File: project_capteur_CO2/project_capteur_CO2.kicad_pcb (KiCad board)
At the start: 2 copper layers, 9 parts, among them U1 ESP32_NODEMCU, U2 DHT11

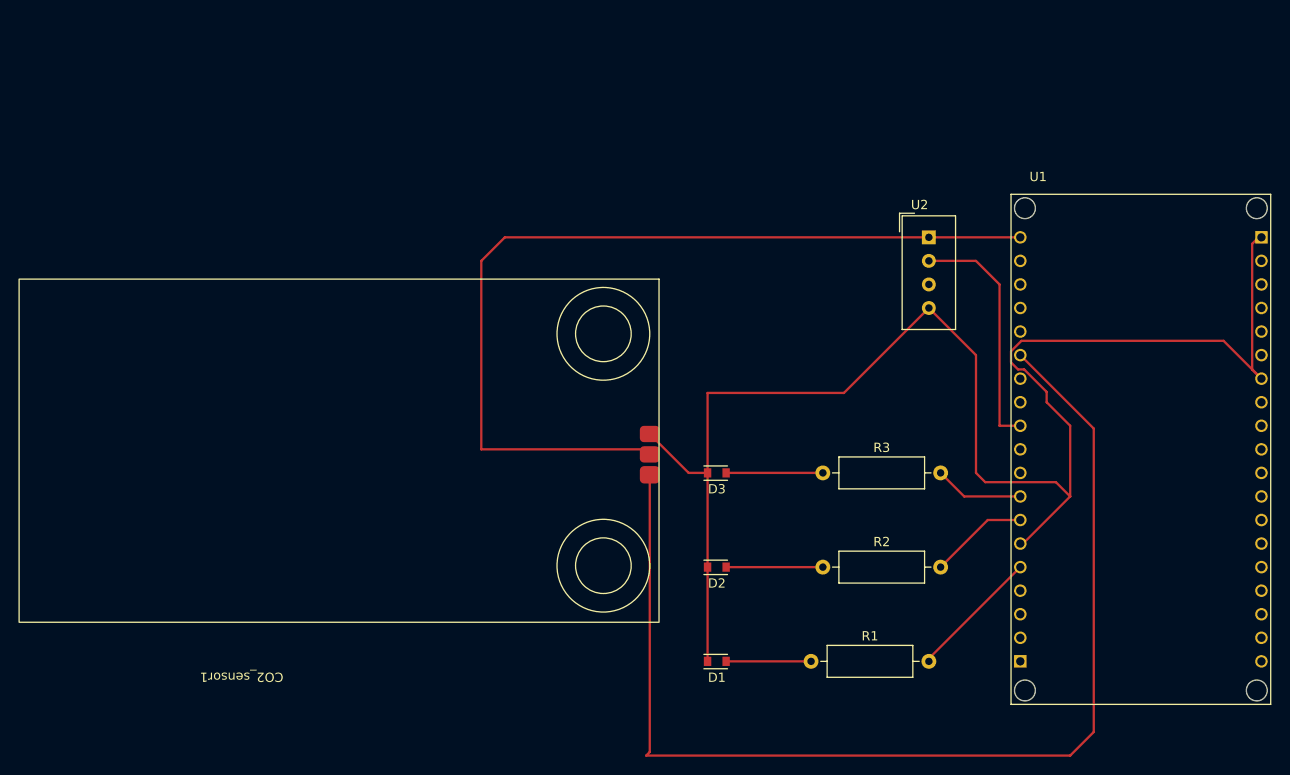
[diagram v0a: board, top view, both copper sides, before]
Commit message: pinheader - coorection led empreinte ajouter
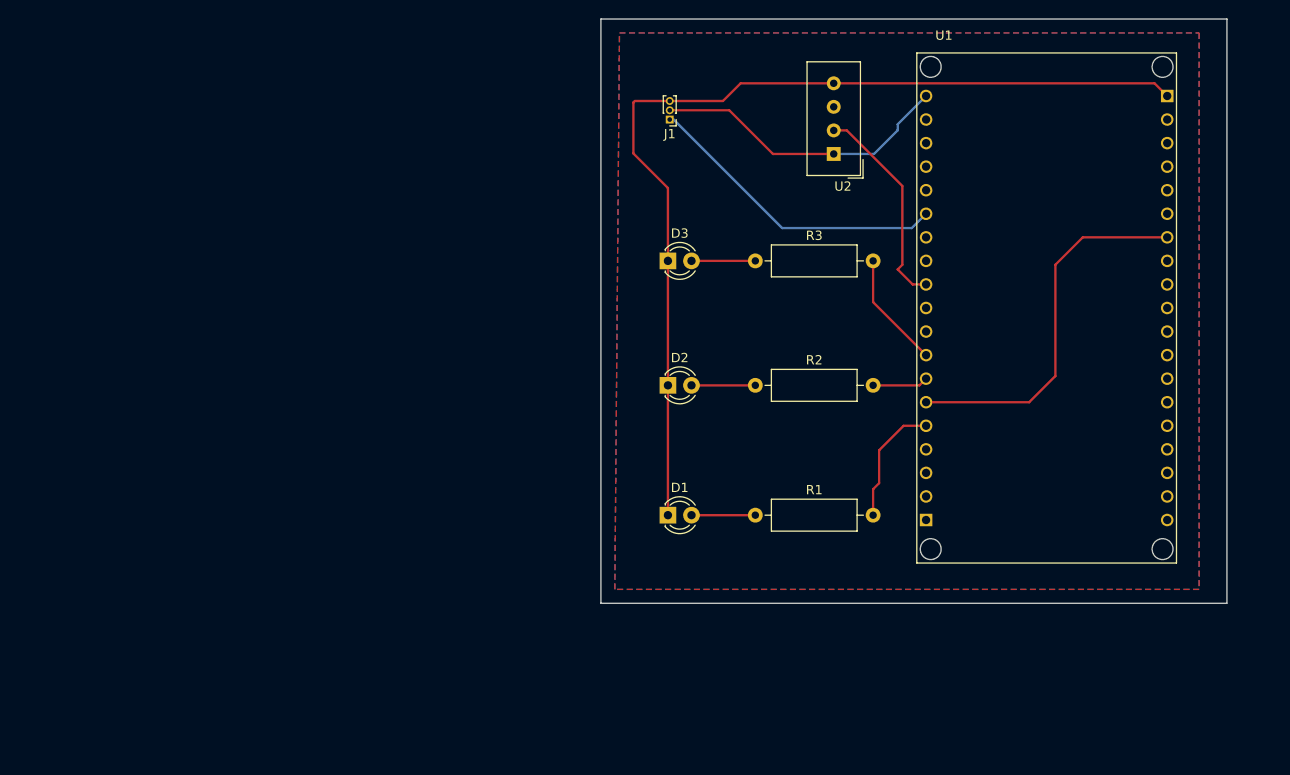
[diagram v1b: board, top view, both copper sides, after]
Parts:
- removed CO2_sensor1: Gravity_infrared_CO2_sensor_v1.2, Gravity infrared co2 sensor v1:Sensor_CO2_3pins_37mmx69mm
- added J1: Pinheader, Connector_PinHeader_1.00mm:PinHeader_1x03_P1.00mm_Vertical, F.Cu at (185.4, 53.3)
- D1, D2, D3: footprint LED_SMD:LED_miniPLCC_2315 -> LED_THT:LED_D3.0mm
- moved R3 24.0 mm to (194.7, 68.6)
- moved D3 23.5 mm to (185.2, 68.6)
- moved R2 20.9 mm to (194.7, 82.0)
- moved D2 20.3 mm to (185.2, 82.0)
- moved U1 18.3 mm to (226.1, 73.7)
- moved R1 16.9 mm to (194.7, 96.0)
- moved D1 16.6 mm to (185.2, 96.0)
- moved U2 13.6 mm to (203.1, 57.1), turned to 180 degrees
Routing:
- net Net-(J1-Pad1): track 123.7 -> 33.1 mm
- net Net-(J1-Pad2): track 97.9 -> 32.6 mm
- net GND: track 167.2 -> 145.4 mm
- net Net-(R2-Pad2): track 10.7 -> 6.01 mm
- net Net-(D3-Pad2): track 10.4 -> 6.89 mm
- net Net-(D2-Pad2): track 10.4 -> 6.89 mm
- net Net-(U1-PadJ5_11): track 26.2 -> 22.8 mm
- net Net-(R3-Pad2): track 9.64 -> 12.5 mm
- net Net-(D1-Pad2): track 9.16 -> 6.89 mm
- net Net-(R1-Pad2): track 14.2 -> 13.4 mm
- added copper zone on B.Cu, net GND
- added copper zone on F.Cu, net GND
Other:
- board outline added: 67.5 x 63 mm
